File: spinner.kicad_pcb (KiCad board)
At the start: 2 copper layers, 147 x 147 mm, 107 parts, among them J1 Micro_SD_Card, SW1 SW_SPDT, U1 AP63205WU, U2 RS0102, U3 SFH617A-3X006, U4 SFH617A-3X006, U5 SFH617A-3X006, U6 ESP32-S3-WROOM-1

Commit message: IDK.  Add LDO n stuff.
Issue:  HAKZ-100
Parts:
- removed U6: ESP32-S3-WROOM-1, Library:ESP32-S3-WROOM-1
- added J301: USB_C_Receptacle_USB2.0_16P, Connector_USB:USB_C_Receptacle_GCT_USB4105-xx-A_16P_TopMnt_Horizontal, F.Cu at (214.8, 76.4)
- added R306: 5.1k, Resistor_SMD:R_0603_1608Metric, F.Cu at (208.0, 80.0)
- added R307: 5.1k, Resistor_SMD:R_0603_1608Metric, F.Cu at (207.0, 77.3)
- added U301: BQ24073RGT, Package_DFN_QFN:VQFN-16-1EP_3x3mm_P0.5mm_EP1.6x1.6mm, F.Cu at (63.8, 43.6)
- added u10: ESP32-S3-WROOM-1, Library:ESP32-S3-WROOM-1, F.Cu at (150.0, 54.0)
- I1, I2: value IDC -> 1
- moved RN1 133.7 mm to (165.5, 151.4), turned to 0 degrees
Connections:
- BT1 pad 2: Net-(BT1-Pad2) -> GND
- BT2 pad 1: Net-(BT1-Pad2) -> +BATT
- BT2 pad 2: Net-(BT2-Pad2) -> GND
- BT3 pad 1: Net-(BT2-Pad2) -> +BATT

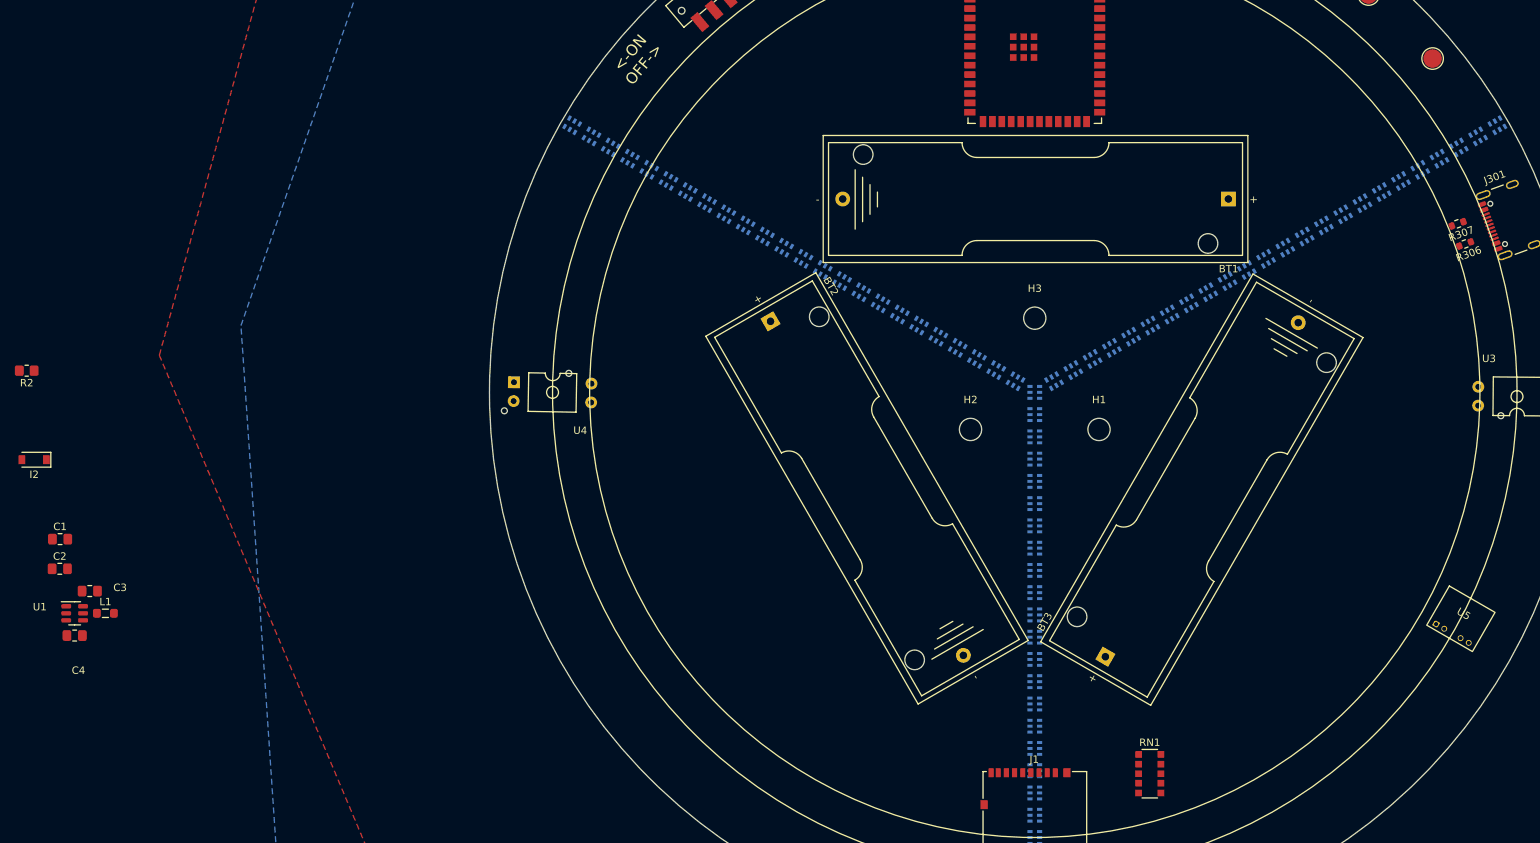
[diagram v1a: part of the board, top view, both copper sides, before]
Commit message: Decided to ditch the bounce beam.  Added labels to SD and USB.
Amazing resitor layout.  Ditched resitor network.
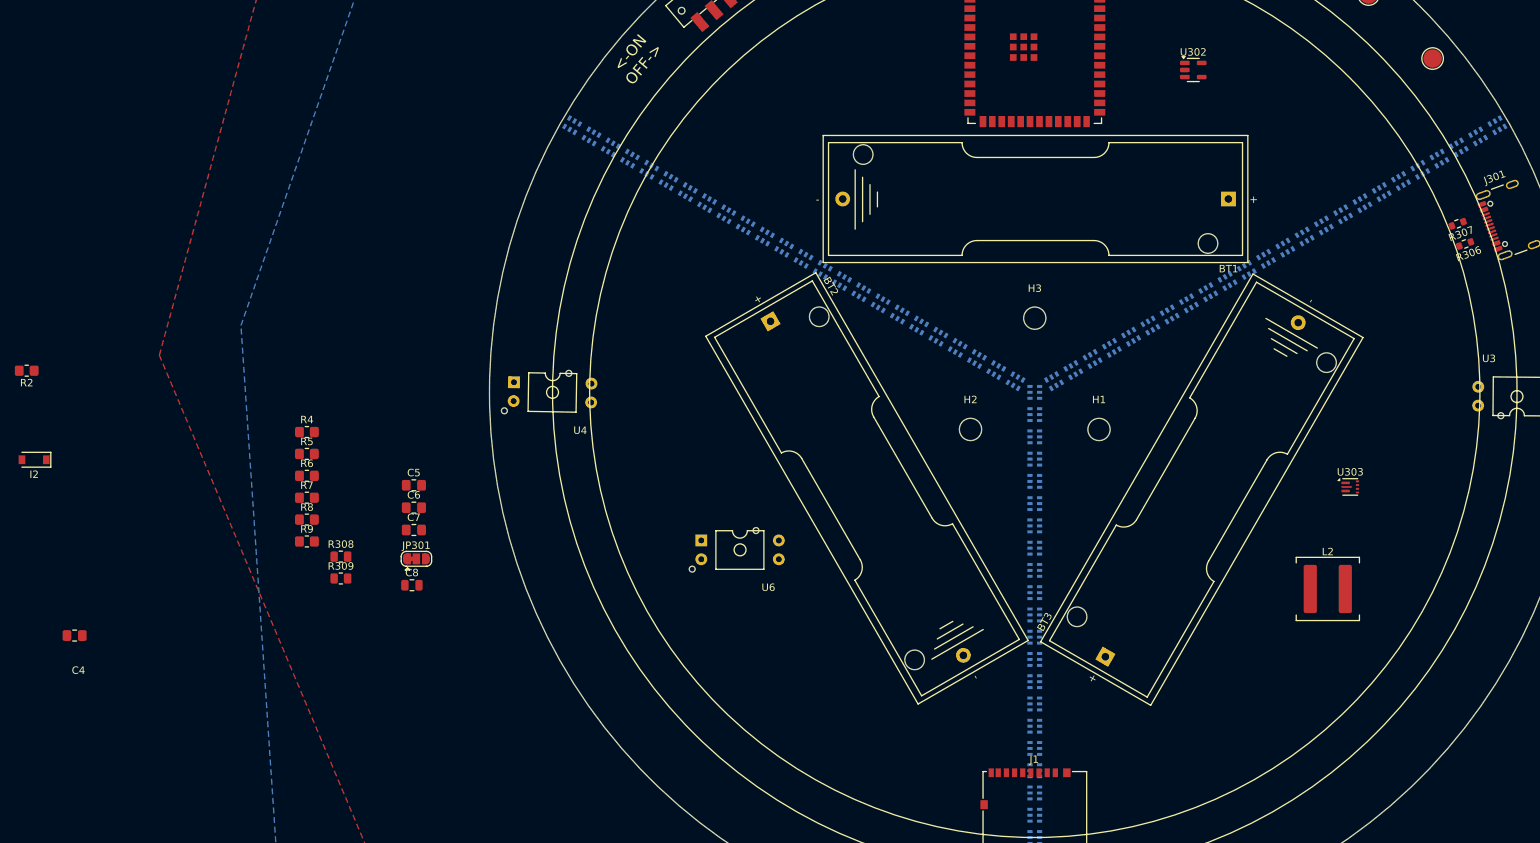
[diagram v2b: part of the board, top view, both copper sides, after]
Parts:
- removed C1, C2: 22uF, Capacitor_SMD:C_0805_2012Metric_Pad1.18x1.45mm_HandSolder
- removed C3: .1uF, Capacitor_SMD:C_0805_2012Metric_Pad1.18x1.45mm_HandSolder
- removed L1: 4.7uH, Inductor_SMD:L_0805_2012Metric_Pad1.05x1.20mm_HandSolder
- removed RN1: R_Network08, Resistor_SMD:R_Array_Convex_5x1206
- removed U1: AP63205WU, Package_TO_SOT_SMD:TSOT-23-6
- removed U5: SFH617A-3X006, Library:tcrt1000
- added C5: 10uF, Capacitor_SMD:C_0805_2012Metric_Pad1.18x1.45mm_HandSolder, F.Cu at (66.3, 112.5)
- added C6: 22uF, Capacitor_SMD:C_0805_2012Metric_Pad1.18x1.45mm_HandSolder, F.Cu at (66.3, 115.5)
- added C7: 22uF, Capacitor_SMD:C_0805_2012Metric_Pad1.18x1.45mm_HandSolder, F.Cu at (66.3, 118.5)
- added C8: 10nF, Capacitor_SMD:C_0805_2012Metric, F.Cu at (66.0, 126.0)
- added JP301: SolderJumper_3_Bridged12, Jumper:SolderJumper-3_P1.3mm_Bridged12_RoundedPad1.0x1.5mm, F.Cu at (66.7, 122.4)
- added L2: 1 uH, Inductor_SMD:L_Coilcraft_XAL7030-102, F.Cu at (189.5, 126.5)
- added R308: 732k, Resistor_SMD:R_0805_2012Metric, F.Cu at (56.5, 122.1)
- added R309: 100k, Resistor_SMD:R_0805_2012Metric, F.Cu at (56.5, 125.1)
- added R4: 10k, Resistor_SMD:R_0805_2012Metric_Pad1.20x1.40mm_HandSolder, F.Cu at (51.9, 105.3)
- added R5: 10k, Resistor_SMD:R_0805_2012Metric_Pad1.20x1.40mm_HandSolder, F.Cu at (51.9, 108.3)
- added R6: 10k, Resistor_SMD:R_0805_2012Metric_Pad1.20x1.40mm_HandSolder, F.Cu at (51.9, 111.2)
- added R7: 10k, Resistor_SMD:R_0805_2012Metric_Pad1.20x1.40mm_HandSolder, F.Cu at (51.9, 114.2)
- added R8: 10k, Resistor_SMD:R_0805_2012Metric_Pad1.20x1.40mm_HandSolder, F.Cu at (51.9, 117.2)
- added R9: 10k, Resistor_SMD:R_0805_2012Metric_Pad1.20x1.40mm_HandSolder, F.Cu at (51.9, 120.1)
- added U302: SPX3819M5-L-3-3, Package_TO_SOT_SMD:SOT-23-5, F.Cu at (171.4, 56.5)
- added U303: TPS61022, Package_DFN_QFN:Texas_RWU0007A_VQFN-7_2x2mm_P0.5mm, F.Cu at (192.5, 112.8)
- added U6: SFH617A-3X006, Library:MULTI_PART_THRU_BEAM, F.Cu at (110.3, 121.2)
- C4: value 10uF -> 22uF
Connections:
- BT1 pad 1: +BATT -> Net-(BT1-+)
- BT2 pad 1: +BATT -> Net-(BT1-+)
- BT3 pad 1: +BATT -> Net-(BT1-+)
- C4 pad 1: Net-(SW1-C) -> +5V
- J1 pad 1: Net-(J1-DAT2) -> /dat_2
- J1 pad 2: /spi_cs -> /dat_3
- J1 pad 3: /spi_out -> /cmd
- J1 pad 7: /spi_in -> /dat_0
- J1 pad 8: Net-(J1-DAT1) -> /dat_1
- J301 pad A4: Net-(J301-VBUS-PadA4) -> V USB
- J301 pad A9: Net-(J301-VBUS-PadA4) -> V USB
- J301 pad B4: Net-(J301-VBUS-PadA4) -> V USB
- J301 pad B9: Net-(J301-VBUS-PadA4) -> V USB
- SW1 pad 1: unconnected-(SW1-A-Pad1) -> GND
- SW1 pad 2: +BATT -> Net-(SW1-B)
- SW1 pad 3: Net-(SW1-C) -> BATT_COND
- U2 pad 6: /GPIO_14 -> unconnected-(U2-A2-Pad6)
- U2 pad 7: /GPIO_13 -> unconnected-(U2-A1-Pad7)
- U301 pad 10: Net-(R304-Pad1) -> BATT_COND
- U301 pad 11: Net-(R304-Pad1) -> BATT_COND
- U301 pad 13: unconnected-(U301-IN-Pad13) -> V USB
- U301 pad 5: +3V3 -> +BATT

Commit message: Did the things... and happiness.
Placed through beam, boost circuit layout, labeled done things.
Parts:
- added I3: 1, Diode_SMD:D_SOD-123, F.Cu at (16.9, 119.0)
- moved C4 185.8 mm to (206.0, 121.5), turned to -90 degrees
- moved R308 146.2 mm to (202.5, 115.5), turned to -90 degrees
- moved R309 143.4 mm to (199.5, 115.5), turned to 90 degrees
- moved C7 141.7 mm to (208.0, 121.5), turned to -90 degrees
- moved C6 137.8 mm to (204.0, 121.5), turned to -90 degrees
- moved U2 135.6 mm to (133.0, 60.0)
- moved C5 130.5 mm to (196.5, 121.0), turned to 90 degrees
- moved JP301 127.5 mm to (194.0, 116.5)
- moved C8 123.5 mm to (166.1, 53.5)
- moved R4 118.3 mm to (163.0, 146.1)
- moved R5 118.3 mm to (163.0, 149.1)
- moved R6 118.3 mm to (163.0, 152.0)
- moved R7 118.3 mm to (163.0, 154.9)
- moved R8 118.3 mm to (163.0, 157.9)
- moved R9 118.3 mm to (163.0, 160.8)
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- renumbered U3 to TB1, U4 to TB2, U6 to TB3
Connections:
- TB1 pad 2: Net-(U3-Pad2) -> GND
- TB3 pad 1: Net-(U3-Pad2) -> Net-(I3-Pad2)

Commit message: Add a datasheet and make a few connections.  etc.
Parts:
- removed I1, I2, I3: 1, Diode_SMD:D_SOD-123
- added D327: D_Current-regulator, Diode_SMD:D_SOD-123, F.Cu at (205.2, 98.5)
- added D328: D_Current-regulator, Diode_SMD:D_SOD-123, F.Cu at (95.0, 102.0)
- added D329: D_Current-regulator, Diode_SMD:D_SOD-123, F.Cu at (119.5, 130.5)
- moved R3 173.7 mm to (97.0, 119.0), turned to -150 degrees
- moved U301 139.5 mm to (197.2, 83.9)
- moved R2 80.9 mm to (95.0, 97.5)
- moved R1 59.8 mm to (219.5, 107.0), turned to 90 degrees
- moved R9 23.7 mm to (145.0, 145.5), turned to -90 degrees
- moved R8 20.2 mm to (147.0, 145.5), turned to -90 degrees
- moved R7 16.9 mm to (149.0, 145.5), turned to -90 degrees
- moved R6 13.6 mm to (151.0, 145.5), turned to -90 degrees
- moved R5 10.6 mm to (153.0, 145.5), turned to -90 degrees
- moved R4 8.02 mm to (155.0, 145.5), turned to -90 degrees
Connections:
- D0 pad 6: Net-(D0-DO) -> /DI
- D101 pad 1: Net-(D0-DO) -> /DI

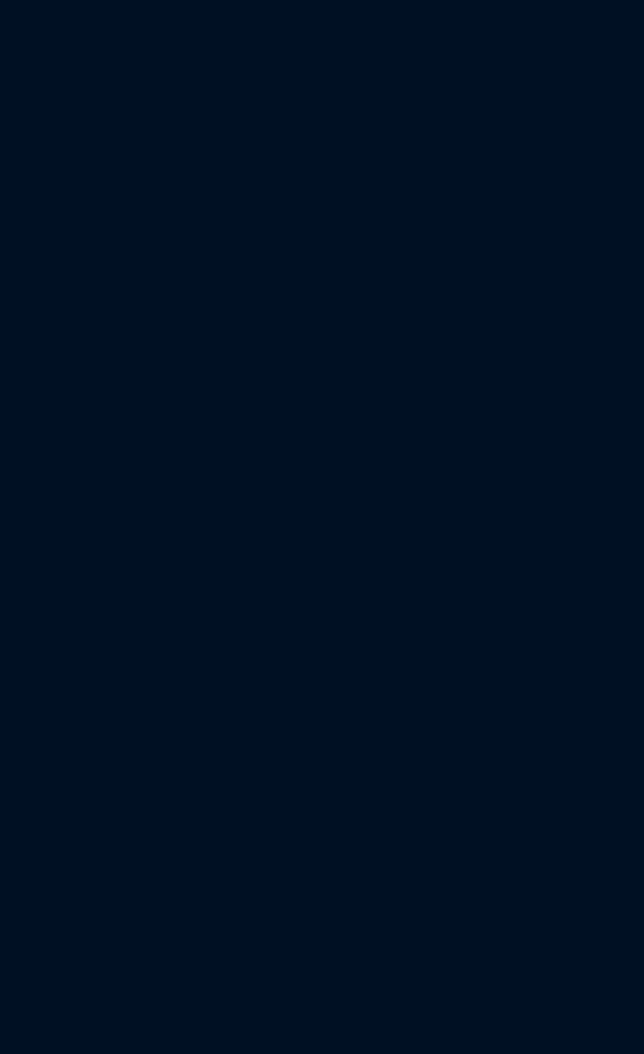
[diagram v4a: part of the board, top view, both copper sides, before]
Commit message: Added touch pads.
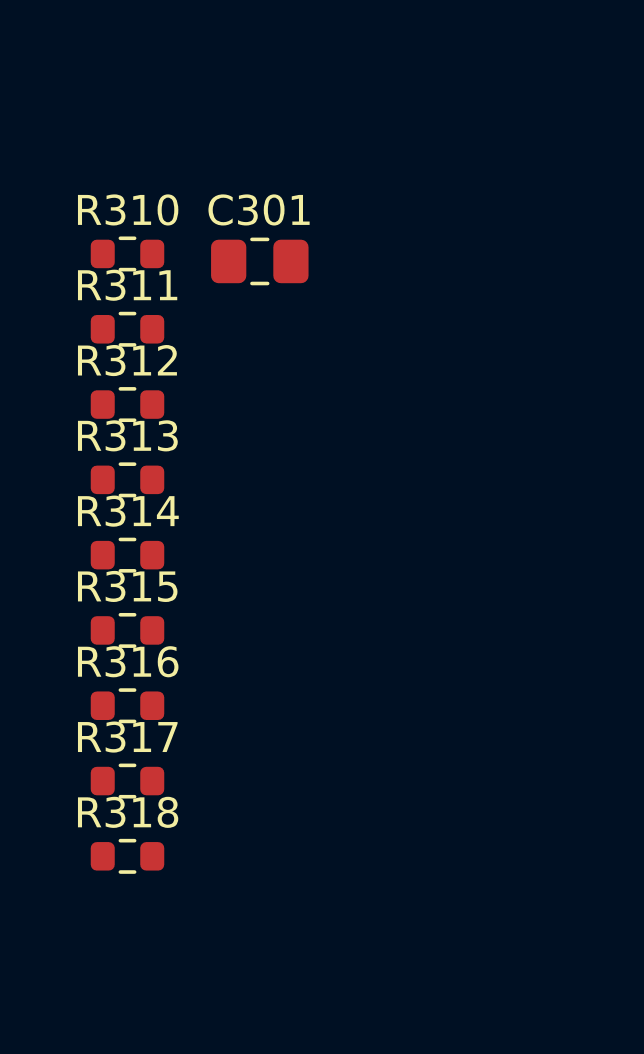
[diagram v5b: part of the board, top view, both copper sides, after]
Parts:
- added C301: 1uF, Capacitor_SMD:C_0805_2012Metric_Pad1.18x1.45mm_HandSolder, F.Cu at (10.6, 10.7)
- added R310: 5.1k, Resistor_SMD:R_0603_1608Metric, F.Cu at (6.17, 10.5)
- added R311: 510, Resistor_SMD:R_0603_1608Metric, F.Cu at (6.17, 13.0)
- added R312: 510, Resistor_SMD:R_0603_1608Metric, F.Cu at (6.17, 15.5)
- added R313: 510, Resistor_SMD:R_0603_1608Metric, F.Cu at (6.17, 18.0)
- added R314: 510, Resistor_SMD:R_0603_1608Metric, F.Cu at (6.17, 20.5)
- added R315: 510, Resistor_SMD:R_0603_1608Metric, F.Cu at (6.17, 23.0)
- added R316: 510, Resistor_SMD:R_0603_1608Metric, F.Cu at (6.17, 25.5)
- added R317: 510, Resistor_SMD:R_0603_1608Metric, F.Cu at (6.17, 28.0)
- added R318: 510, Resistor_SMD:R_0603_1608Metric, F.Cu at (6.17, 30.5)
- TP4: value VCC -> 5VCC
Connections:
- net /CHG_L renamed Net-(D325-K)
- net /PGOOD_L renamed Net-(D326-K)
- D0 pad 4: VCC -> +5V
- D0 pad 6: /DI -> Net-(D0-DO)
- D101 pad 1: /DI -> Net-(D0-DO)
- D101 pad 4: VCC -> +5V
- D102 pad 4: VCC -> +5V
- D103 pad 4: VCC -> +5V
- D104 pad 4: VCC -> +5V
- D105 pad 4: VCC -> +5V
- D106 pad 4: VCC -> +5V
- D107 pad 4: VCC -> +5V
- D108 pad 4: VCC -> +5V
- D109 pad 4: VCC -> +5V
- D110 pad 4: VCC -> +5V
- D111 pad 4: VCC -> +5V
- D112 pad 4: VCC -> +5V
- D113 pad 4: VCC -> +5V
- D114 pad 4: VCC -> +5V
- D115 pad 4: VCC -> +5V
- D116 pad 4: VCC -> +5V
- D117 pad 4: VCC -> +5V
- D118 pad 4: VCC -> +5V
- D119 pad 4: VCC -> +5V
- D120 pad 4: VCC -> +5V
- D121 pad 4: VCC -> +5V
- D122 pad 4: VCC -> +5V
- D123 pad 4: VCC -> +5V
- D124 pad 4: VCC -> +5V
- D201 pad 4: VCC -> +5V
- D202 pad 4: VCC -> +5V
- D203 pad 4: VCC -> +5V
- D204 pad 4: VCC -> +5V
- D205 pad 4: VCC -> +5V
- D206 pad 4: VCC -> +5V
- D207 pad 4: VCC -> +5V
- D208 pad 4: VCC -> +5V
- D209 pad 4: VCC -> +5V
- D210 pad 4: VCC -> +5V
- D211 pad 4: VCC -> +5V
- D212 pad 4: VCC -> +5V
- D213 pad 4: VCC -> +5V
- D214 pad 4: VCC -> +5V
- D215 pad 4: VCC -> +5V
- D216 pad 4: VCC -> +5V
- D217 pad 4: VCC -> +5V
- D218 pad 4: VCC -> +5V
- D219 pad 4: VCC -> +5V
- D220 pad 4: VCC -> +5V
- D221 pad 4: VCC -> +5V
- D222 pad 4: VCC -> +5V
- D223 pad 4: VCC -> +5V
- D224 pad 4: VCC -> +5V
- D301 pad 4: VCC -> +5V
- D302 pad 4: VCC -> +5V
- D303 pad 4: VCC -> +5V
- D304 pad 4: VCC -> +5V
- D305 pad 4: VCC -> +5V
- D306 pad 4: VCC -> +5V
- D307 pad 4: VCC -> +5V
- D308 pad 4: VCC -> +5V
- D309 pad 4: VCC -> +5V
- D310 pad 4: VCC -> +5V
- D311 pad 4: VCC -> +5V
- D312 pad 4: VCC -> +5V
- D313 pad 4: VCC -> +5V
- D314 pad 4: VCC -> +5V
- D315 pad 4: VCC -> +5V
- D316 pad 4: VCC -> +5V
- D317 pad 4: VCC -> +5V
- D318 pad 4: VCC -> +5V
- D319 pad 4: VCC -> +5V
- D320 pad 4: VCC -> +5V
- D321 pad 4: VCC -> +5V
- D322 pad 4: VCC -> +5V
- D323 pad 4: VCC -> +5V
- D324 pad 4: VCC -> +5V
- D327 pad 2: VCC -> +5V
- D328 pad 2: VCC -> +5V
- D329 pad 2: VCC -> +5V
- TP4 pad 1: VCC -> +5V
- U2 pad 1: VCC -> +5V
- U2 pad 6: unconnected-(U2-A2-Pad6) -> /CI_3v3
- U2 pad 7: unconnected-(U2-A1-Pad7) -> /DI_3v3
- u10 pad 1: Net-(u10-GND-Pad1) -> GND
- u10 pad 10: unconnected-(u10-GPIO17/U1TXD/ADC2_CH6-Pad10) -> /DI_3v3
- u10 pad 11: unconnected-(u10-GPIO18/U1RXD/ADC2_CH7/CLK_OUT3-Pad11) -> /CI_3v3
- u10 pad 12: unconnected-(u10-GPIO8/TOUCH8/ADC1_CH7/SUBSPICS1-Pad12) -> /touch_pad_08
- u10 pad 15: unconnected-(u10-GPIO3/TOUCH3/ADC1_CH2-Pad15) -> /touch_pad_03
- u10 pad 17: unconnected-(u10-GPIO9/TOUCH9/ADC1_CH8/FSPIHD/SUBSPIHD-Pad17) -> /spi_clk
- u10 pad 18: unconnected-(u10-GPIO10/TOUCH10/ADC1_CH9/FSPICS0/FSPIIO4/SUBSPICS0-Pad18) -> /cmd
- u10 pad 19: unconnected-(u10-GPIO11/TOUCH11/ADC2_CH0/FSPID/FSPIIO5/SUBSPID-Pad19) -> /dat_0
- u10 pad 2: unconnected-(u10-3V3-Pad2) -> +3V3
- u10 pad 20: unconnected-(u10-GPIO12/TOUCH12/ADC2_CH1/FSPICLK/FSPIIO6/SUBSPICLK-Pad20) -> /dat_1
- u10 pad 21: unconnected-(u10-GPIO13/TOUCH13/ADC2_CH2/FSPIQ/FSPIIO7/SUBSPIQ-Pad21) -> /dat_2
- u10 pad 22: unconnected-(u10-GPIO14/TOUCH14/ADC2_CH3/FSPIWP/FSPIDQS/SUBSPIWP-Pad22) -> /dat_3
- u10 pad 27: unconnected-(u10-GPIO0/BOOT-Pad27) -> Net-(u10-GPIO0/BOOT)
- u10 pad 3: unconnected-(u10-EN-Pad3) -> Net-(u10-EN)
- u10 pad 32: unconnected-(u10-MTCK/GPIO39/CLK_OUT3/SUBSPICS1-Pad32) -> /OPTO_in_0
- u10 pad 33: unconnected-(u10-MTDO/GPIO40/CLK_OUT2-Pad33) -> /OPTO_in_1
- u10 pad 34: unconnected-(u10-MTDI/GPIO41/CLK_OUT1-Pad34) -> /OPTO_in_2
- u10 pad 38: unconnected-(u10-GPIO2/TOUCH2/ADC1_CH1-Pad38) -> /touch_pad_02
- u10 pad 39: unconnected-(u10-GPIO1/TOUCH1/ADC1_CH0-Pad39) -> /touch_pad_01
- u10 pad 4: unconnected-(u10-GPIO4/TOUCH4/ADC1_CH3-Pad4) -> /touch_pad_04
- u10 pad 40: Net-(u10-GND-Pad1) -> GND
- u10 pad 41: Net-(u10-GND-Pad1) -> GND
- u10 pad 5: unconnected-(u10-GPIO5/TOUCH5/ADC1_CH4-Pad5) -> /touch_pad_05
- u10 pad 6: unconnected-(u10-GPIO6/TOUCH6/ADC1_CH5-Pad6) -> /touch_pad_06
- u10 pad 7: unconnected-(u10-GPIO7/TOUCH7/ADC1_CH6-Pad7) -> /touch_pad_07
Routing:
- added copper zone on F.Cu, net +5V
- removed copper zone on F.Cu, net VCC

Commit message: Adding recent work.  schematic & layout are done-ish
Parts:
- removed R316, R317, R318: 510, Resistor_SMD:R_0603_1608Metric
- added D325: LED, LED_SMD:LED_0805_2012Metric, F.Cu at (206.0, 86.0)
- added D326: LED, LED_SMD:LED_0805_2012Metric, F.Cu at (206.0, 89.6)
- added SW301: RESET, Button_Switch_SMD:SW_Push_SPST_NO_Alps_SKRK, F.Cu at (121.1, 50.2)
- added SW302: BOOT, Button_Switch_SMD:SW_Push_SPST_NO_Alps_SKRK, F.Cu at (128.6, 46.8)
- added TP309: TestPoint_2Pole, Library:TouchSlider-2_20x10mm, B.Cu at (179.1, 50.6)
- R1, R2, R3: value ~3.3k -> 3.3k
- R313, R314, R315: value 510 -> 1k
- moved R312 162.1 mm to (164.9, 48.2)
- moved R311 159.4 mm to (161.9, 46.7)
- moved R310 136.2 mm to (137.6, 45.9), turned to 180 degrees
- moved R313 135.8 mm to (141.4, 31.1)
- moved C301 132.3 mm to (137.6, 47.8)
- moved R314 124.3 mm to (129.7, 34.1)
- moved R315 113.6 mm to (118.6, 39.4)
- moved C7 16.2 mm to (193.4, 128.4), turned to 180 degrees
- moved C4 13.5 mm to (193.4, 126.4), turned to 180 degrees
- moved L2 13.3 mm to (187.9, 118.9), turned to -90 degrees
- moved C6 11.0 mm to (193.4, 124.4), turned to 180 degrees
- moved R308 8.08 mm to (199.4, 122.9), turned to 180 degrees
- moved U303 7.41 mm to (193.6, 121.5), turned to 90 degrees
- moved R3 5.42 mm to (98.0, 124.3)
- moved C5 4.83 mm to (193.9, 116.9), turned to 0 degrees
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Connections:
- R313 pad 1: /touch_pad_03 -> Net-(R313-Pad1)
- R313 pad 2: Net-(R313-Pad2) -> +3V3
- R314 pad 1: /touch_pad_04 -> Net-(R314-Pad1)
- R314 pad 2: Net-(R314-Pad2) -> +5V
- R315 pad 1: /touch_pad_05 -> Net-(R315-Pad1)
- R315 pad 2: Net-(R315-Pad2) -> +BATT
- TP3 pad 1: +3V3 -> Net-(R313-Pad1)
- TP4 pad 1: +5V -> Net-(R314-Pad1)
- TP9 pad 1: +BATT -> Net-(R315-Pad1)
- u10 pad 12: /touch_pad_08 -> unconnected-(u10-GPIO8/TOUCH8/ADC1_CH7/SUBSPICS1-Pad12)
- u10 pad 15: /touch_pad_03 -> unconnected-(u10-GPIO3/TOUCH3/ADC1_CH2-Pad15)
- u10 pad 4: /touch_pad_04 -> unconnected-(u10-GPIO4/TOUCH4/ADC1_CH3-Pad4)
- u10 pad 5: /touch_pad_05 -> unconnected-(u10-GPIO5/TOUCH5/ADC1_CH4-Pad5)
- u10 pad 6: /touch_pad_06 -> unconnected-(u10-GPIO6/TOUCH6/ADC1_CH5-Pad6)
- u10 pad 7: /touch_pad_07 -> unconnected-(u10-GPIO7/TOUCH7/ADC1_CH6-Pad7)
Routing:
- net Net-(D102-DO): track 0.00 -> 1.40 mm
- net Net-(D102-CO): track 0.00 -> 1.40 mm

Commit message: IDK.  Some routing.
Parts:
- moved D101 3.00 mm to (150.0, 100.0)
- moved D0 3.00 mm to (150.0, 103.0)
- renumbered D101 to D0, D0 to D101
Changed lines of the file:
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@@
 	(footprint "Library:SK9822-hakz"
 		(layer "B.Cu")
-		(at 150 103)
+		(at 150 100)
 		(descr "http://www.led-color.com/upload/201604/APA102-2020%20SMD%20LED.pdf")
 		(tags "LED RGB SPI")
-		(property "Reference" "D0"
+		(property "Reference" "D101"
 			(at 0 -2.11 0)
 			(layer "B.SilkS")
@@
 	(footprint "Library:SK9822-hakz"
 		(layer "B.Cu")
-		(at 150 100)
+		(at 150 102.9972)
 		(descr "http://www.led-color.com/upload/201604/APA102-2020%20SMD%20LED.pdf")
 		(tags "LED RGB SPI")
-		(property "Reference" "D101"
+		(property "Reference" "D0"
 			(at 0 -2.11 0)
 			(layer "B.SilkS")
